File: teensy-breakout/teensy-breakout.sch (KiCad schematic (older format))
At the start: 2 parts

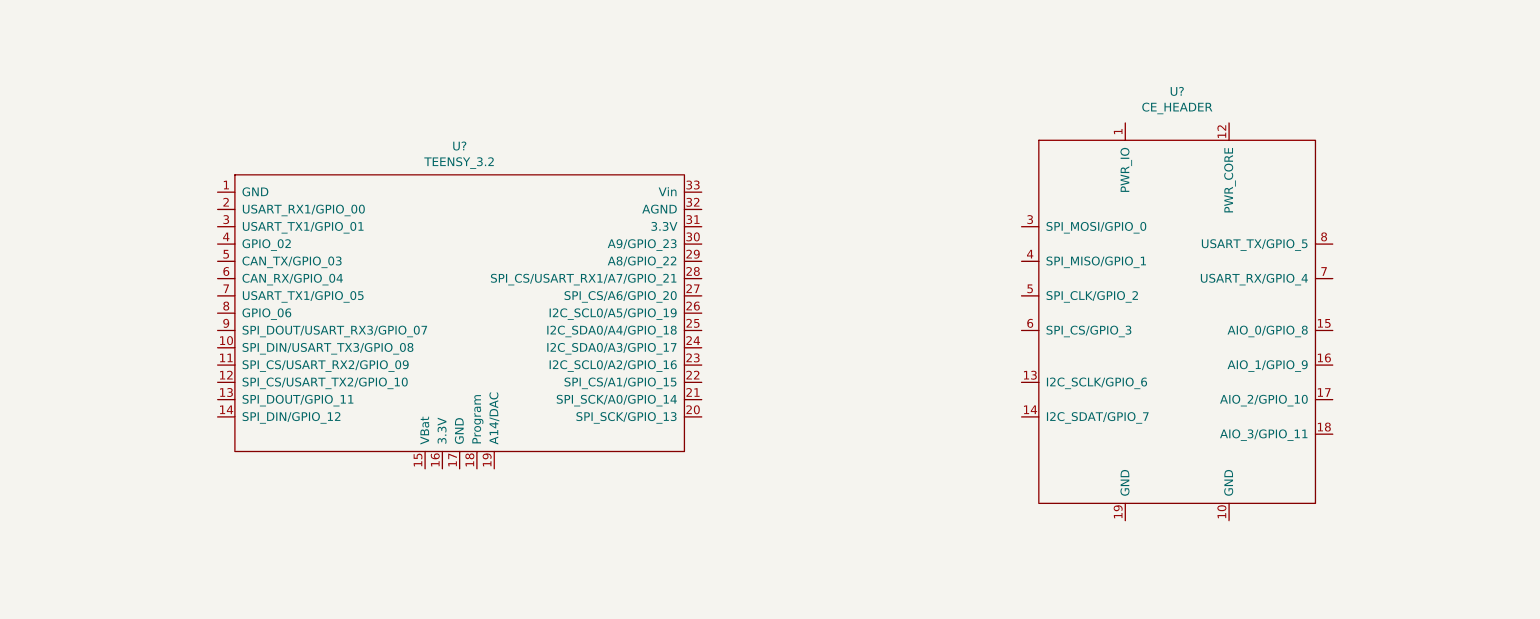
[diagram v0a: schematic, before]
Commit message: Connected Teensy breakout to CE header
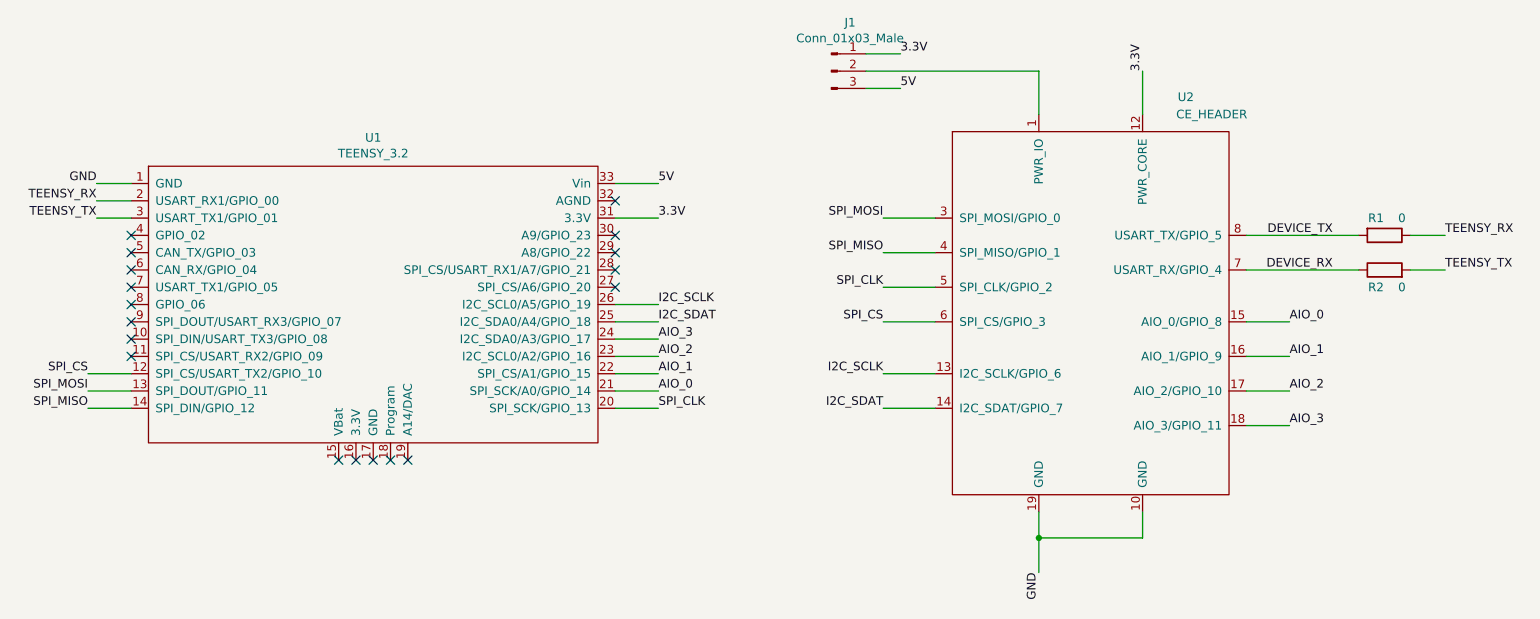
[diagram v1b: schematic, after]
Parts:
- added J1: Conn_01x03_Male, symbol Connector:Conn_01x03_Male
- added R1, R2: 0, symbol Device:R
- gave numbers to parts that had none: 2
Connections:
- net GND: now reaches U1.1 (GND)
- net GND: now also U2.10 (GND), U2.19 (GND)
- net SPI_CS: now reaches U1.12 (SPI_CS/USART_TX2/GPIO_10)
- net SPI_CS: now also U2.6 (SPI_CS/GPIO_3)
- net SPI_MOSI: now reaches U1.13 (SPI_DOUT/GPIO_11)
- net SPI_MOSI: now also U2.3 (SPI_MOSI/GPIO_0)
- net SPI_MISO: now reaches U1.14 (SPI_DIN/GPIO_12)
- net SPI_MISO: now also U2.4 (SPI_MISO/GPIO_1)
- net TEENSY_RX: now reaches U1.2 (USART_RX1/GPIO_00)
- net TEENSY_RX: now also R1.1
- net SPI_CLK: now reaches U1.20 (SPI_SCK/GPIO_13)
- net SPI_CLK: now also U2.5 (SPI_CLK/GPIO_2)
- net AIO_0: now reaches U1.21 (SPI_SCK/A0/GPIO_14)
- net AIO_0: now also U2.15 (AIO_0/GPIO_8)
- net AIO_1: now reaches U1.22 (SPI_CS/A1/GPIO_15)
- net AIO_1: now also U2.16 (AIO_1/GPIO_9)
- net AIO_2: now reaches U1.23 (I2C_SCL0/A2/GPIO_16)
- net AIO_2: now also U2.17 (AIO_2/GPIO_10)
- net AIO_3: now reaches U1.24 (I2C_SDA0/A3/GPIO_17)
- net AIO_3: now also U2.18 (AIO_3/GPIO_11)
- net I2C_SDAT: now reaches U1.25 (I2C_SDA0/A4/GPIO_18)
- net I2C_SDAT: now also U2.14 (I2C_SDAT/GPIO_7)
- net I2C_SCLK: now reaches U1.26 (I2C_SCL0/A5/GPIO_19)
- net I2C_SCLK: now also U2.13 (I2C_SCLK/GPIO_6)
- net TEENSY_TX: now reaches U1.3 (USART_TX1/GPIO_01)
- net TEENSY_TX: now also R2.2
- net 3.3V: now reaches U1.31 (3.3V)
- net 3.3V: now also U2.12 (PWR_CORE), J1.1 (Pin_1)
- net 5V: now reaches U1.33 (Vin)
- net 5V: now also J1.3 (Pin_3)
- net at U2.1 (PWR_IO): now also J1.2 (Pin_2)
- net DEVICE_RX: now reaches U2.7 (USART_RX/GPIO_4)
- net DEVICE_RX: now also R2.1
- net DEVICE_TX: now reaches U2.8 (USART_TX/GPIO_5)
- net DEVICE_TX: now also R1.2
- no-connect marks 0 -> 18
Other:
- moved on the sheet: U1, U2
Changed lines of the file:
@@
 $EndDescr
 $Comp
-L teensy-breakout:TEENSY_3.2 U?
+L teensy-breakout:TEENSY_3.2 U1
 U 1 1 5E4C5F79
-P 4000 3700
-F 0 "U?" H 4000 4665 50  0000 C CNN
-F 1 "TEENSY_3.2" H 4000 4574 50  0000 C CNN
-F 2 "" H 4000 3700 50  0001 C CNN
-F 3 "" H 4000 3700 50  0001 C CNN
-	1    4000 3700
+P 3500 3650
+F 0 "U1" H 3500 4615 50  0000 C CNN
+F 1 "TEENSY_3.2" H 3500 4524 50  0000 C CNN
+F 2 "" H 3500 3650 50  0001 C CNN
+F 3 "" H 3500 3650 50  0001 C CNN
+	1    3500 3650
 	1    0    0    -1
 $EndComp
 $Comp
-L ce-header:CE_HEADER U?
+L ce-header:CE_HEADER U2
 U 1 1 5E4C70BC
-P 8150 3800
-F 0 "U?" H 8150 5181 50  0000 C CNN
-F 1 "CE_HEADER" H 8150 5090 50  0000 C CNN
-F 2 "" H 8150 3700 50  0001 C CNN
-F 3 "" H 8150 3700 50  0001 C CNN
-	1    8150 3800
+P 7650 3750
+F 0 "U2" H 8200 5050 50  0000 C CNN
+F 1 "CE_HEADER" H 8350 4950 50  0000 C CNN
+F 2 "" H 7650 3650 50  0001 C CNN
+F 3 "" H 7650 3650 50  0001 C CNN
+	1    7650 3750
 	1    0    0    -1
 $EndComp
+Text Label 5150 3150 0    50   ~ 0
+3.3V
+$Comp
+L Connector:Conn_01x03_Male J1
+U 1 1 5E3ECD4D
+P 6150 2300
+F 0 "J1" H 6258 2581 50  0000 C CNN
+F 1 "Conn_01x03_Male" H 6258 2490 50  0000 C CNN
+F 2 "" H 6150 2300 50  0001 C CNN
+F 3 "~" H 6150 2300 50  0001 C CNN
+	1    6150 2300
+	1    0    0    -1
+$EndComp
+Wire Wire Line
+	7350 2550 7350 2300
+Wire Wire Line
+	7350 2300 6350 2300
+Wire Wire Line
+	7950 2550 7950 2300
+Text Label 7950 2300 1    50   ~ 0
+3.3V
+Text Label 5150 2950 0    50   ~ 0
+5V
+Wire Wire Line
+	6350 2400 6550 2400
+Wire Wire Line
+	6350 2200 6550 2200
+Text Label 6550 2200 0    50   ~ 0
+3.3V
+Text Label 6550 2400 0    50   ~ 0
+5V
+Wire Wire Line
+	7350 4850 7350 5000
+Text Label 7350 5200 3    50   ~ 0
+GND
+Wire Wire Line
+	7950 4850 7950 5000
+Wire Wire Line
+	7950 5000 7350 5000
+Connection ~ 7350 5000
+Wire Wire Line
+	7350 5000 7350 5200
+Text Label 1900 2950 2    50   ~ 0
+GND
+Wire Wire Line
+	6750 3150 6450 3150
+Wire Wire Line
+	6750 3350 6450 3350
+Wire Wire Line
+	6750 3550 6450 3550
+Wire Wire Line
+	6750 3750 6450 3750
+Text Label 6450 3150 2    50   ~ 0
+SPI_MOSI
+Text Label 6450 3350 2    50   ~ 0
+SPI_MISO
+Text Label 6450 3550 2    50   ~ 0
+SPI_CLK
+Text Label 6450 3750 2    50   ~ 0
+SPI_CS
+Text Label 1850 4050 2    50   ~ 0
+SPI_CS
+Wire Wire Line
+	2100 4050 1850 4050
+Text Label 5150 4250 0    50   ~ 0
+SPI_CLK
+Wire Wire Line
+	4900 4250 5150 4250
+Wire Wire Line
+	2100 4150 1850 4150
+Wire Wire Line
+	2100 4250 1850 4250
+Text Label 1850 4150 2    50   ~ 0
+SPI_MOSI
+Text Label 1850 4250 2    50   ~ 0
+SPI_MISO
+$Comp
+L Device:R R1
+U 1 1 5E3F19B0
+P 9350 3250
+F 0 "R1" V 9250 3200 50  0000 C CNN
+F 1 "0" V 9250 3350 50  0000 C CNN
+F 2 "" V 9280 3250 50  0001 C CNN
+F 3 "~" H 9350 3250 50  0001 C CNN
+	1    9350 3250
+	0    1    1    0
+$EndComp
+$Comp
+L Device:R R2
+U 1 1 5E3F2057
+P 9350 3450
+F 0 "R2" V 9250 3500 50  0000 C CNN
+F 1 "0" V 9250 3350 50  0000 C CNN
+F 2 "" V 9280 3450 50  0001 C CNN
+F 3 "~" H 9350 3450 50  0001 C CNN
+	1    9350 3450
+	0    -1   -1   0
+$EndComp
+Wire Wire Line
+	9500 3250 9700 3250
+Wire Wire Line
+	9500 3450 9700 3450
+Wire Wire Line
+	2100 3050 1900 3050
+Wire Wire Line
+	2100 3150 1900 3150
+Text Label 9700 3250 0    50   ~ 0
+TEENSY_RX
+Text Label 9050 3250 2    50   ~ 0
+DEVICE_TX
+Wire Wire Line
+	8550 3250 9200 3250
+Wire Wire Line
+	8550 3450 9200 3450
+Text Label 9050 3450 2    50   ~ 0
+DEVICE_RX
+Text Label 9700 3450 0    50   ~ 0
+TEENSY_TX
+Text Label 1900 3050 2    50   ~ 0
+TEENSY_RX
+Text Label 1900 3150 2    50   ~ 0
+TEENSY_TX
+Wire Wire Line
+	6750 4050 6450 4050
+Wire Wire Line
+	6750 4250 6450 4250
+Text Label 6450 4050 2    50   ~ 0
+I2C_SCLK
+Text Label 6450 4250 2    50   ~ 0
+I2C_SDAT
+Wire Wire Line
+	4900 3650 5150 3650
+Wire Wire Line
+	4900 3750 5150 3750
+Text Label 5150 3650 0    50   ~ 0
+I2C_SCLK
+Text Label 5150 3750 0    50   ~ 0
+I2C_SDAT
+Wire Wire Line
+	4900 3850 5150 3850
+Wire Wire Line
+	4900 3950 5150 3950
+Wire Wire Line
+	4900 4050 5150 4050
+Wire Wire Line
+	4900 4150 5150 4150
+Wire Wire Line
+	8550 3750 8800 3750
+Wire Wire Line
+	8550 3950 8800 3950
+Wire Wire Line
+	8550 4150 8800 4150
+Wire Wire Line
+	8550 4350 8800 4350
+Text Label 8800 3750 0    50   ~ 0
+AIO_0
+Text Label 8800 3950 0    50   ~ 0
+AIO_1
+Text Label 8800 4150 0    50   ~ 0
+AIO_2
+Text Label 8800 4350 0    50   ~ 0
+AIO_3
+Text Label 5150 4150 0    50   ~ 0
+AIO_0
+Text Label 5150 4050 0    50   ~ 0
+AIO_1
+Text Label 5150 3950 0    50   ~ 0
+AIO_2
+Text Label 5150 3850 0    50   ~ 0
+AIO_3
+NoConn ~ 4900 3250
+NoConn ~ 4900 3350
+NoConn ~ 4900 3450
+NoConn ~ 4900 3550
+NoConn ~ 2100 3250
+NoConn ~ 2100 3350
+NoConn ~ 2100 3450
+NoConn ~ 2100 3550
+NoConn ~ 2100 3650
+NoConn ~ 2100 3750
+NoConn ~ 2100 3850
+NoConn ~ 2100 3950
+NoConn ~ 3500 4550
+NoConn ~ 3600 4550
+NoConn ~ 3700 4550
+NoConn ~ 3400 4550
+NoConn ~ 3300 4550
+NoConn ~ 4900 3050
+Wire Wire Line
+	4900 2950 5150 2950
+Wire Wire Line
+	4900 3150 5150 3150
+Wire Wire Line
+	1900 2950 2100 2950
 $EndSCHEMATC

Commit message: Teensy breakout board
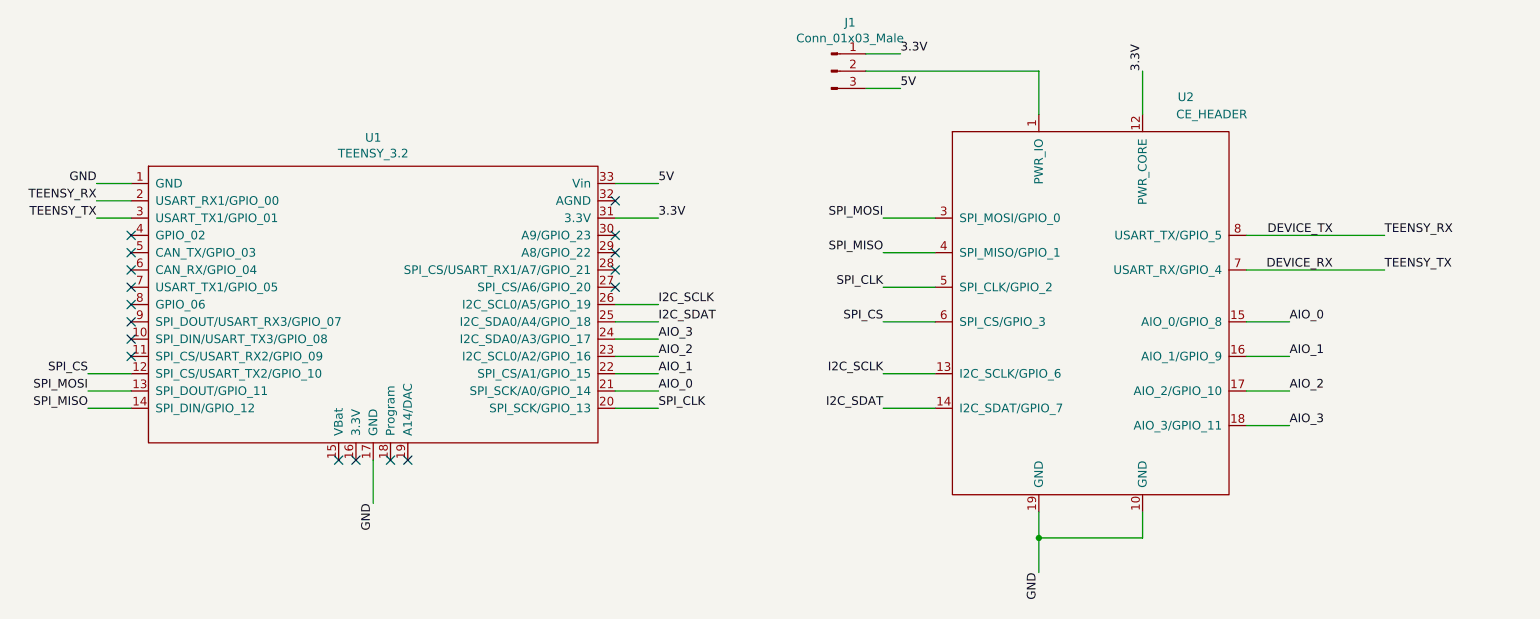
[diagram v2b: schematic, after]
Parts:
- removed R1, R2: 0, symbol Device:R
- J1: footprint (none) -> Connector_PinHeader_2.54mm:PinHeader_1x03_P2.54mm_Vertical
- U1: footprint (none) -> teensy-breakout:TEENSY_3.2
- U2: footprint (none) -> ce-header:CE_Header_Converter
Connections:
- net TEENSY_RX is gone; now on net DEVICE_TX: U1.2 (USART_RX1/GPIO_00)
- net TEENSY_TX is gone; now on net DEVICE_RX: U1.3 (USART_TX1/GPIO_01)
- net GND: now also U1.17 (GND)
- no-connect marks 18 -> 17
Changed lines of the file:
@@
 F 0 "U1" H 3500 4615 50  0000 C CNN
 F 1 "TEENSY_3.2" H 3500 4524 50  0000 C CNN
-F 2 "" H 3500 3650 50  0001 C CNN
+F 2 "teensy-breakout:TEENSY_3.2" H 3500 3650 50  0001 C CNN
 F 3 "" H 3500 3650 50  0001 C CNN
 	1    3500 3650
@@
 F 0 "U2" H 8200 5050 50  0000 C CNN
 F 1 "CE_HEADER" H 8350 4950 50  0000 C CNN
-F 2 "" H 7650 3650 50  0001 C CNN
+F 2 "ce-header:CE_Header_Converter" H 7650 3650 50  0001 C CNN
 F 3 "" H 7650 3650 50  0001 C CNN
 	1    7650 3750
@@
 F 0 "J1" H 6258 2581 50  0000 C CNN
 F 1 "Conn_01x03_Male" H 6258 2490 50  0000 C CNN
-F 2 "" H 6150 2300 50  0001 C CNN
+F 2 "Connector_PinHeader_2.54mm:PinHeader_1x03_P2.54mm_Vertical" H 6150 2300 50  0001 C CNN
 F 3 "~" H 6150 2300 50  0001 C CNN
 	1    6150 2300
@@
 Text Label 1850 4250 2    50   ~ 0
 SPI_MISO
-$Comp
-L Device:R R1
-U 1 1 5E3F19B0
-P 9350 3250
-F 0 "R1" V 9250 3200 50  0000 C CNN
-F 1 "0" V 9250 3350 50  0000 C CNN
-F 2 "" V 9280 3250 50  0001 C CNN
-F 3 "~" H 9350 3250 50  0001 C CNN
-	1    9350 3250
-	0    1    1    0
-$EndComp
-$Comp
-L Device:R R2
-U 1 1 5E3F2057
-P 9350 3450
-F 0 "R2" V 9250 3500 50  0000 C CNN
-F 1 "0" V 9250 3350 50  0000 C CNN
-F 2 "" V 9280 3450 50  0001 C CNN
-F 3 "~" H 9350 3450 50  0001 C CNN
-	1    9350 3450
-	0    -1   -1   0
-$EndComp
-Wire Wire Line
-	9500 3250 9700 3250
-Wire Wire Line
-	9500 3450 9700 3450
 Wire Wire Line
 	2100 3050 1900 3050
 Wire Wire Line
 	2100 3150 1900 3150
-Text Label 9700 3250 0    50   ~ 0
+Text Label 9350 3250 0    50   ~ 0
 TEENSY_RX
 Text Label 9050 3250 2    50   ~ 0
 DEVICE_TX
-Wire Wire Line
-	8550 3250 9200 3250
-Wire Wire Line
-	8550 3450 9200 3450
 Text Label 9050 3450 2    50   ~ 0
 DEVICE_RX
-Text Label 9700 3450 0    50   ~ 0
+Text Label 9350 3450 0    50   ~ 0
 TEENSY_TX
 Text Label 1900 3050 2    50   ~ 0
@@
 NoConn ~ 2100 3850
 NoConn ~ 2100 3950
-NoConn ~ 3500 4550
 NoConn ~ 3600 4550
 NoConn ~ 3700 4550
@@
 Wire Wire Line
 	1900 2950 2100 2950
+Wire Wire Line
+	3500 4550 3500 4800
+Text Label 3500 4800 3    50   ~ 0
+GND
+Wire Wire Line
+	8550 3250 9350 3250
+Wire Wire Line
+	8550 3450 9350 3450
 $EndSCHEMATC
